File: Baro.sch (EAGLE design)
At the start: 15 parts, among them IC1 MCP1700T-3302E/TT, IC2 MS563702BA03, Q1 RJU003N03 N-MOSFET, Q2 RJU003N03 N-MOSFET

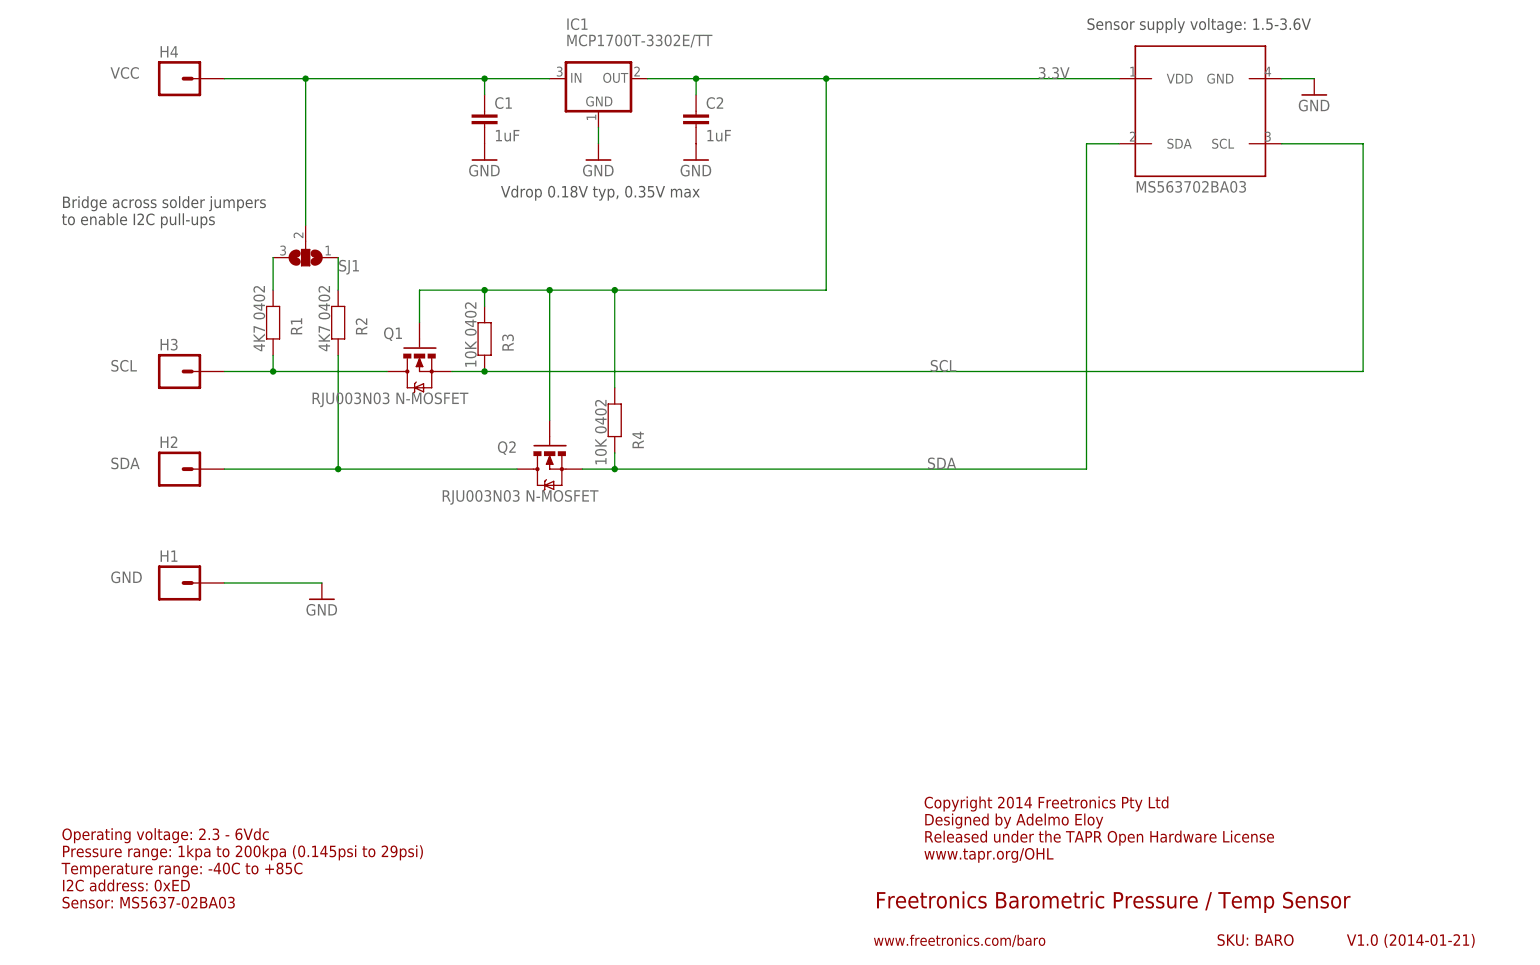
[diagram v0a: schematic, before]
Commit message: Bridged I2C pullup jumpers Shortened URL
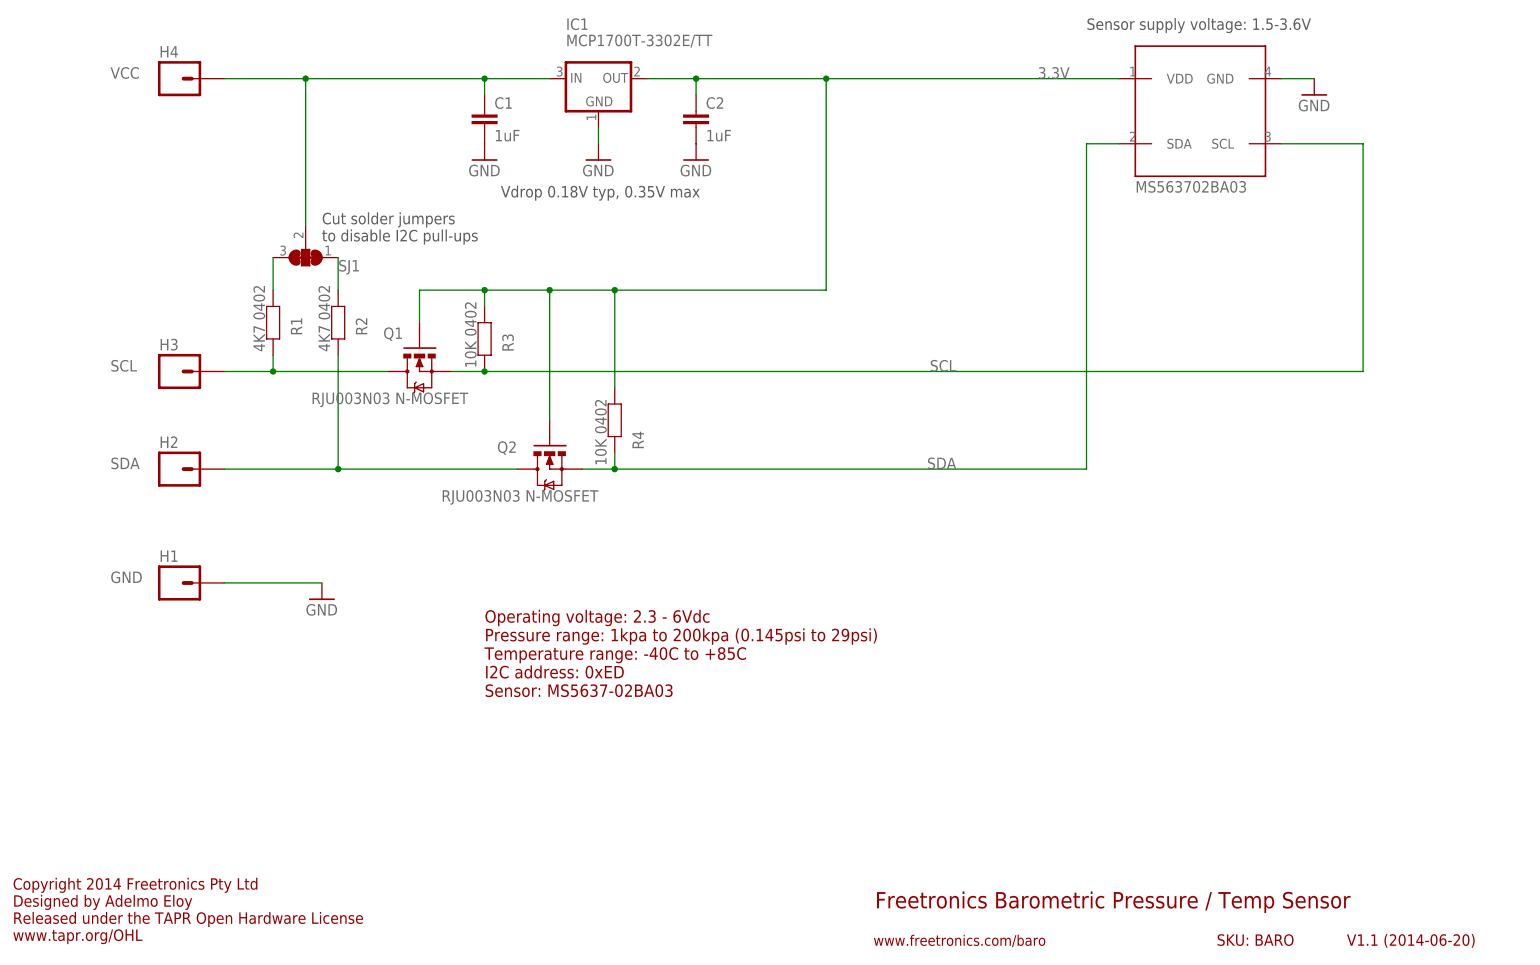
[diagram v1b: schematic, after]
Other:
- note added: "Cut solder jumpers to disable I2C pull-ups"
- note added: "V1.1 (2014-06-20)"
- note removed: "Bridge across solder jumpers to enable I2C pull-ups"
- note removed: "V1.0 (2014-01-21)"
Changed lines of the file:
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@@
 <?xml version="1.0" encoding="utf-8"?>
 <!DOCTYPE eagle SYSTEM "eagle.dtd">
-<eagle version="6.3">
+<eagle version="6.5.0">
 <drawing>
 <settings>
@@
 <plain>
 <text x="142.24" y="12.7" size="2.54" layer="94">Freetronics Barometric Pressure / Temp Sensor</text>
-<text x="215.9" y="6.858" size="1.778" layer="94">V1.0 (2014-01-21)</text>
+<text x="215.9" y="6.858" size="1.778" layer="94">V1.1 (2014-06-20)</text>
 <text x="141.986" y="6.858" size="1.651" layer="94">www.freetronics.com/baro</text>
 <text x="195.58" y="6.858" size="1.778" layer="94">SKU: BARO</text>
@@
 <frame x1="190.5" y1="5.08" x2="213.36" y2="10.16" columns="8" rows="5" layer="94"/>
 <frame x1="213.36" y1="5.08" x2="243.84" y2="10.16" columns="8" rows="5" layer="94"/>
-<text x="15.24" y="119.38" size="1.778" layer="97">Bridge across solder jumpers
-to enable I2C pull-ups</text>
+<text x="55.88" y="116.84" size="1.778" layer="97">Cut solder jumpers
+to disable I2C pull-ups</text>
 <text x="83.82" y="123.698" size="1.778" layer="97">Vdrop 0.18V typ, 0.35V max</text>
-<text x="149.86" y="20.32" size="1.778" layer="94">Copyright 2014 Freetronics Pty Ltd
+<text x="7.62" y="7.62" size="1.778" layer="94">Copyright 2014 Freetronics Pty Ltd
 Designed by Adelmo Eloy
 Released under the TAPR Open Hardware License
 www.tapr.org/OHL</text>
-<text x="15.24" y="12.7" size="1.778" layer="94">Operating voltage: 2.3 - 6Vdc
+<text x="81.28" y="45.72" size="1.9304" layer="94">Operating voltage: 2.3 - 6Vdc
 Pressure range: 1kpa to 200kpa (0.145psi to 29psi)
 Temperature range: -40C to +85C
 I2C address: 0xED
 Sensor: MS5637-02BA03</text>
+<wire x1="50.8" y1="114.3" x2="55.88" y2="114.3" width="0.4064" layer="94"/>
 </plain>
 <instances>
